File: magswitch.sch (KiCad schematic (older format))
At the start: 8 parts

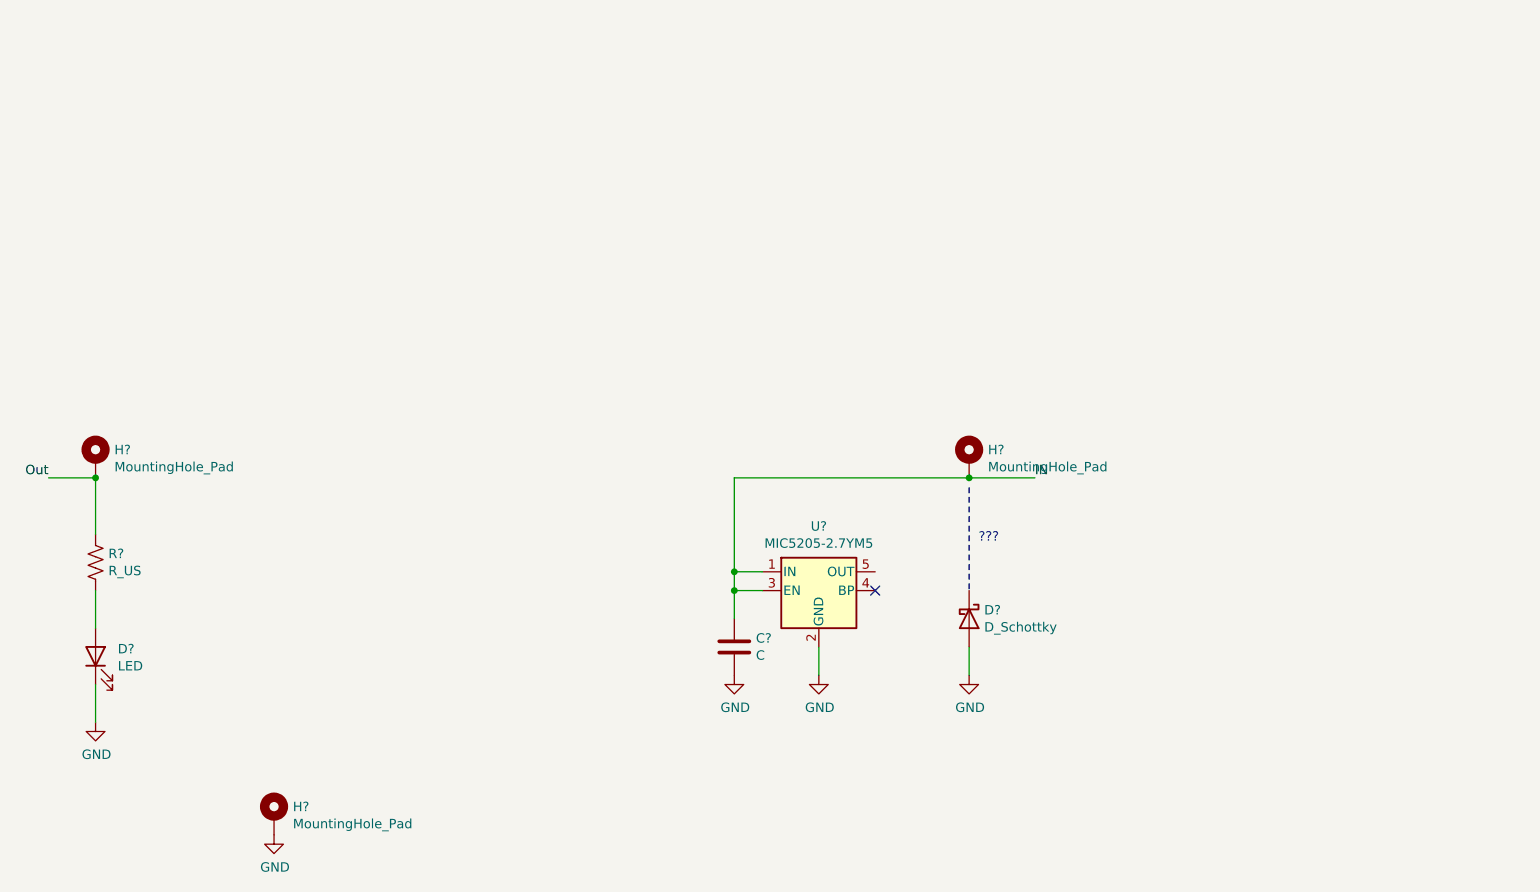
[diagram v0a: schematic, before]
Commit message: Create initial magswitch schematic and layout
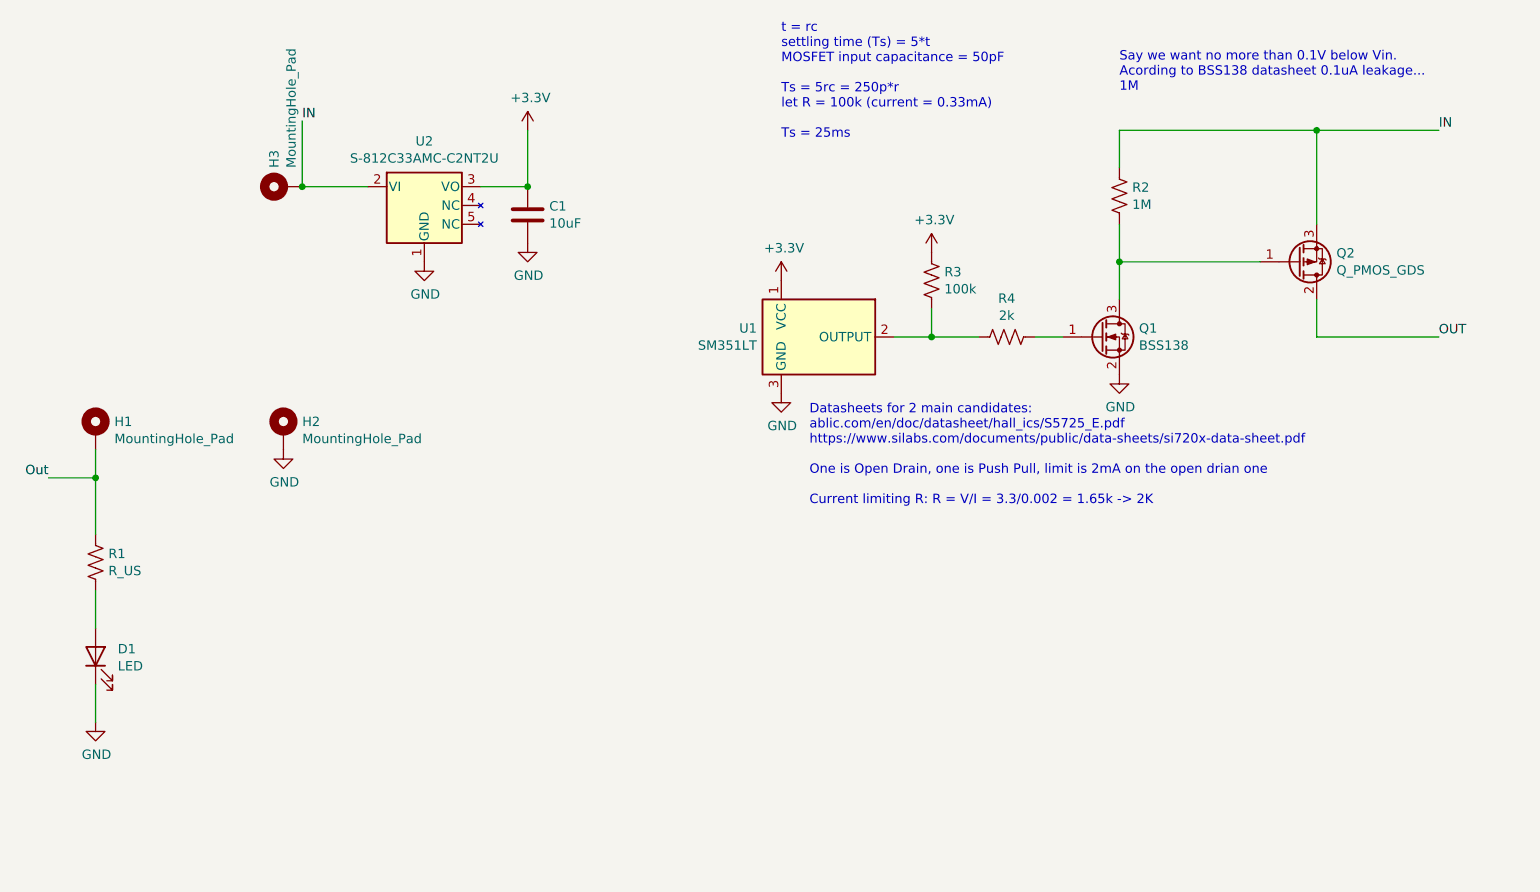
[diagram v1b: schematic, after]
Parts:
- removed C?: C, symbol Device:C
- removed D?: D_Schottky, symbol Device:D_Schottky
- removed U?: MIC5205-2.7YM5, Package_TO_SOT_SMD:SOT-23-5, symbol Regulator_Linear:MIC5205-2.7YM5
- added C1: 10uF, Capacitor_SMD:C_0805_2012Metric, symbol Device:C
- added Q1: BSS138, Package_TO_SOT_SMD:SOT-23, symbol Device:Q_NMOS_GSD
- added Q2: Q_PMOS_GDS, magswitch:SOIC-8_MOSFET, symbol Device:Q_PMOS_GDS
- added R2: 1M, Resistor_SMD:R_0603_1608Metric_Pad1.05x0.95mm_HandSolder, symbol Device:R_US
- added R3: 100k, Resistor_SMD:R_0603_1608Metric_Pad1.05x0.95mm_HandSolder, symbol Device:R_US
- added R4: 2k, Resistor_SMD:R_0603_1608Metric_Pad1.05x0.95mm_HandSolder, symbol Device:R_US
- added U1: SM351LT, Package_TO_SOT_SMD:SOT-23, symbol Sensor_Magnetic:SM351LT
- added U2: S-812C33AMC-C2NT2U, Package_TO_SOT_SMD:SOT-23-5, symbol magswitch:S-812C33AMC-C2NT2U
- D1: renamed from D?; footprint (none) -> LED_SMD:LED_0603_1608Metric_Pad1.05x0.95mm_HandSolder
- H1, H2, H3: renamed from H?; footprint (none) -> MountingHole:MountingHole_3.2mm_M3_Pad_Via
- R1: renamed from R?; footprint (none) -> Resistor_SMD:R_0603_1608Metric
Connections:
- net GND: now also C1.2, Q1.2 (S), U1.3 (GND), U2.1 (GND)
- net IN: now also Q2.3 (S), R2.1, U2.2 (VI)
- new net: Q1.1 (G), R4.1
- new net: Q1.3 (D), Q2.1 (G), R2.2
- new net: R3.2, R4.2, U1.2 (OUTPUT)
- new net +3V3: C1.1, R3.1, U1.1 (VCC), U2.3 (VO)
- new net OUT: Q2.2 (D)
- no-connect marks 1 -> 0
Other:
- note added: "Datasheets for 2 main candidates:\nablic.com/en/doc/datasheet/hall_ics/S5725_E.pdf\nhttps://www.silabs.com/documents/public/data-sheets/si720x-data-sheet.pdf\n\nOne is Open Drain, one is Push Pull, limit is 2mA on the open drian one\n\nCurrent limiting R: R = V/I = 3.3/0.002 = 1.65k -> 2K"
- note added: "Say we want no more than 0.1V below Vin. \nAcording to BSS138 datasheet 0.1uA leakage...\n1M"
- note added: "t = rc\nsettling time (Ts) = 5*t\nMOSFET input capacitance = 50pF\n\nTs = 5rc = 250p*r\nlet R = 100k (current = 0.33mA)\n\nTs = 25ms"
- note removed: "???"
- moved on the sheet: H1, H2, H3

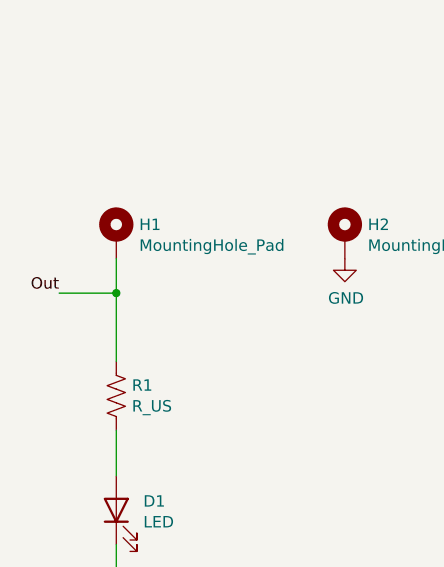
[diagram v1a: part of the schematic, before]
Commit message: Complete board tracing.
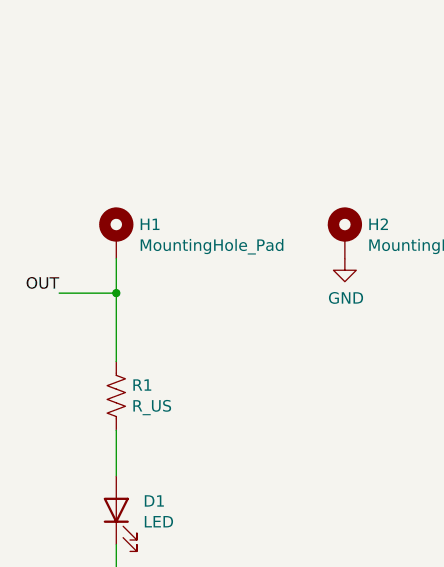
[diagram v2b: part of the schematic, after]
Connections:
- net Out is gone; now on net OUT: H1.1, R1.1
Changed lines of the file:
@@
 	2000 3550 2000 3700
 Text Label 1750 3700 2    50   ~ 0
-Out
+OUT
 $Comp
 L Mechanical:MountingHole_Pad H3

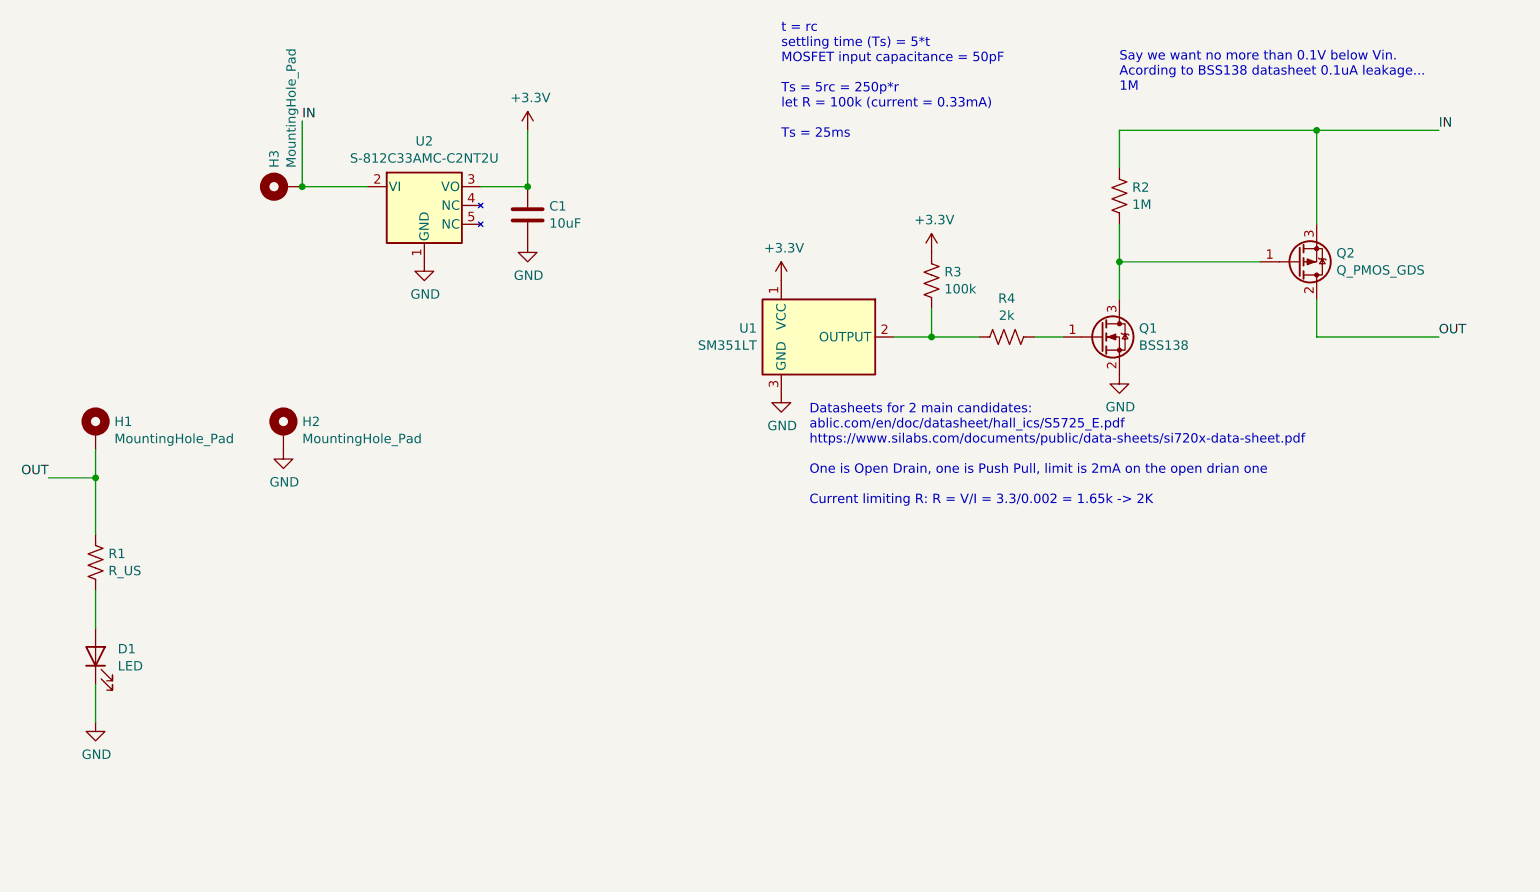
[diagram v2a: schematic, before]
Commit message: Add LED resistor value.
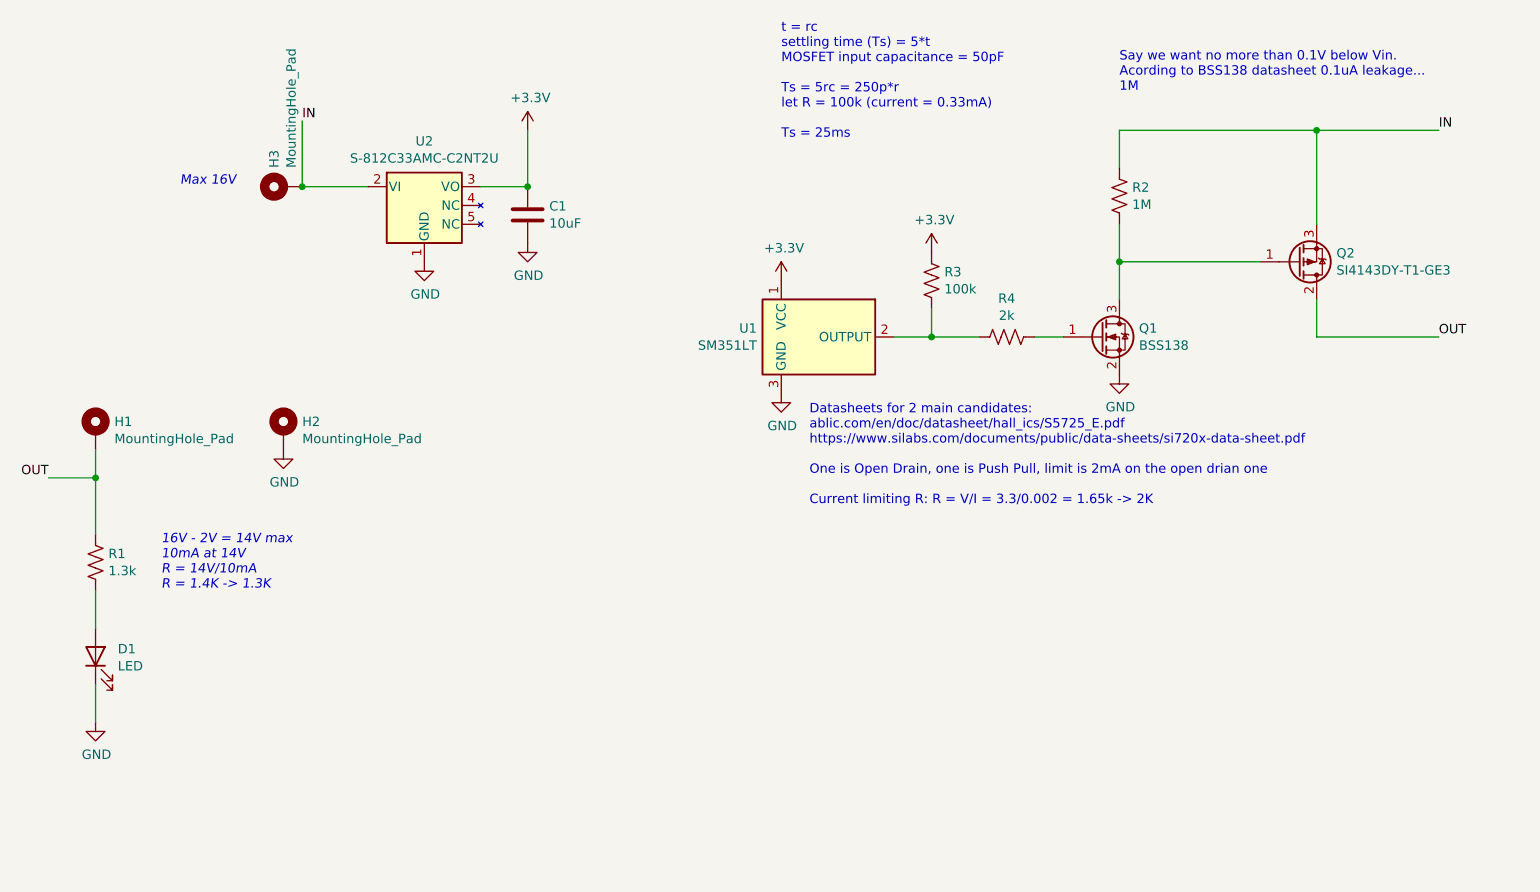
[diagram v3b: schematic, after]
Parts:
- Q2: value Q_PMOS_GDS -> SI4143DY-T1-GE3
- R1: value R_US -> 1.3k
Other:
- note added: "16V - 2V = 14V max\n10mA at 14V\nR = 14V/10mA\nR = 1.4K -> 1.3K\n"
- note added: "Max 16V"
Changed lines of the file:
@@
 F 1 "LED" V 1948 4532 50  0000 R CNN
 F 2 "LED_SMD:LED_0603_1608Metric_Pad1.05x0.95mm_HandSolder" H 2000 4650 50  0001 C CNN
-F 3 "~" H 2000 4650 50  0001 C CNN
+F 3 "https://www.digikey.ca/en/products/detail/w%C3%BCrth-elektronik/150060YS75000/4489909" H 2000 4650 50  0001 C CNN
 	1    2000 4650
 	0    -1   -1   0
@@
 P 2000 4150
 F 0 "R1" H 2068 4196 50  0000 L CNN
-F 1 "R_US" H 2068 4105 50  0000 L CNN
+F 1 "1.3k" H 2068 4105 50  0000 L CNN
 F 2 "Resistor_SMD:R_0603_1608Metric" V 2040 4140 50  0001 C CNN
 F 3 "~" H 2000 4150 50  0001 C CNN
@@
 P 8400 2550
 F 0 "Q2" H 8605 2504 50  0000 L CNN
-F 1 "Q_PMOS_GDS" H 8605 2595 50  0000 L CNN
+F 1 "SI4143DY-T1-GE3" H 8605 2595 50  0000 L CNN
 F 2 "magswitch:SOIC-8_MOSFET" H 8600 2650 50  0001 C CNN
-F 3 "" H 8400 2550 50  0001 C CNN
+F 3 "https://www.digikey.ca/en/products/detail/vishay-siliconix/SI4143DY-T1-GE3/6834464" H 8400 2550 50  0001 C CNN
 	1    8400 2550
 	1    0    0    1
@@
 Wire Wire Line
 	2000 3700 2000 4000
+Text Notes 2450 2150 0    50   Italic 0
+Max 16V
+Text Notes 2350 4300 0    50   Italic 0
+16V - 2V = 14V max\n10mA at 14V\nR = 14V/10mA\nR = 1.4K -> 1.3K\n
 $EndSCHEMATC
